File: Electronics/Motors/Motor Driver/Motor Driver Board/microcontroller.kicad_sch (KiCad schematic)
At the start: 65 parts, among them IC301 TJA1057GT/3, IC302 STM32H723ZGT6, J301 TC2030, J302 Screw_Terminal_01x03, J303 TYPE-C-31-M-12, SW301 SW_DIP_x02, U301 USBLC6-4SC6-ES, U302 LSM6DS3, U303 USBLC6-4SC6-ES, X301 25MHz_Clock, X302 32.768kHz_Clock

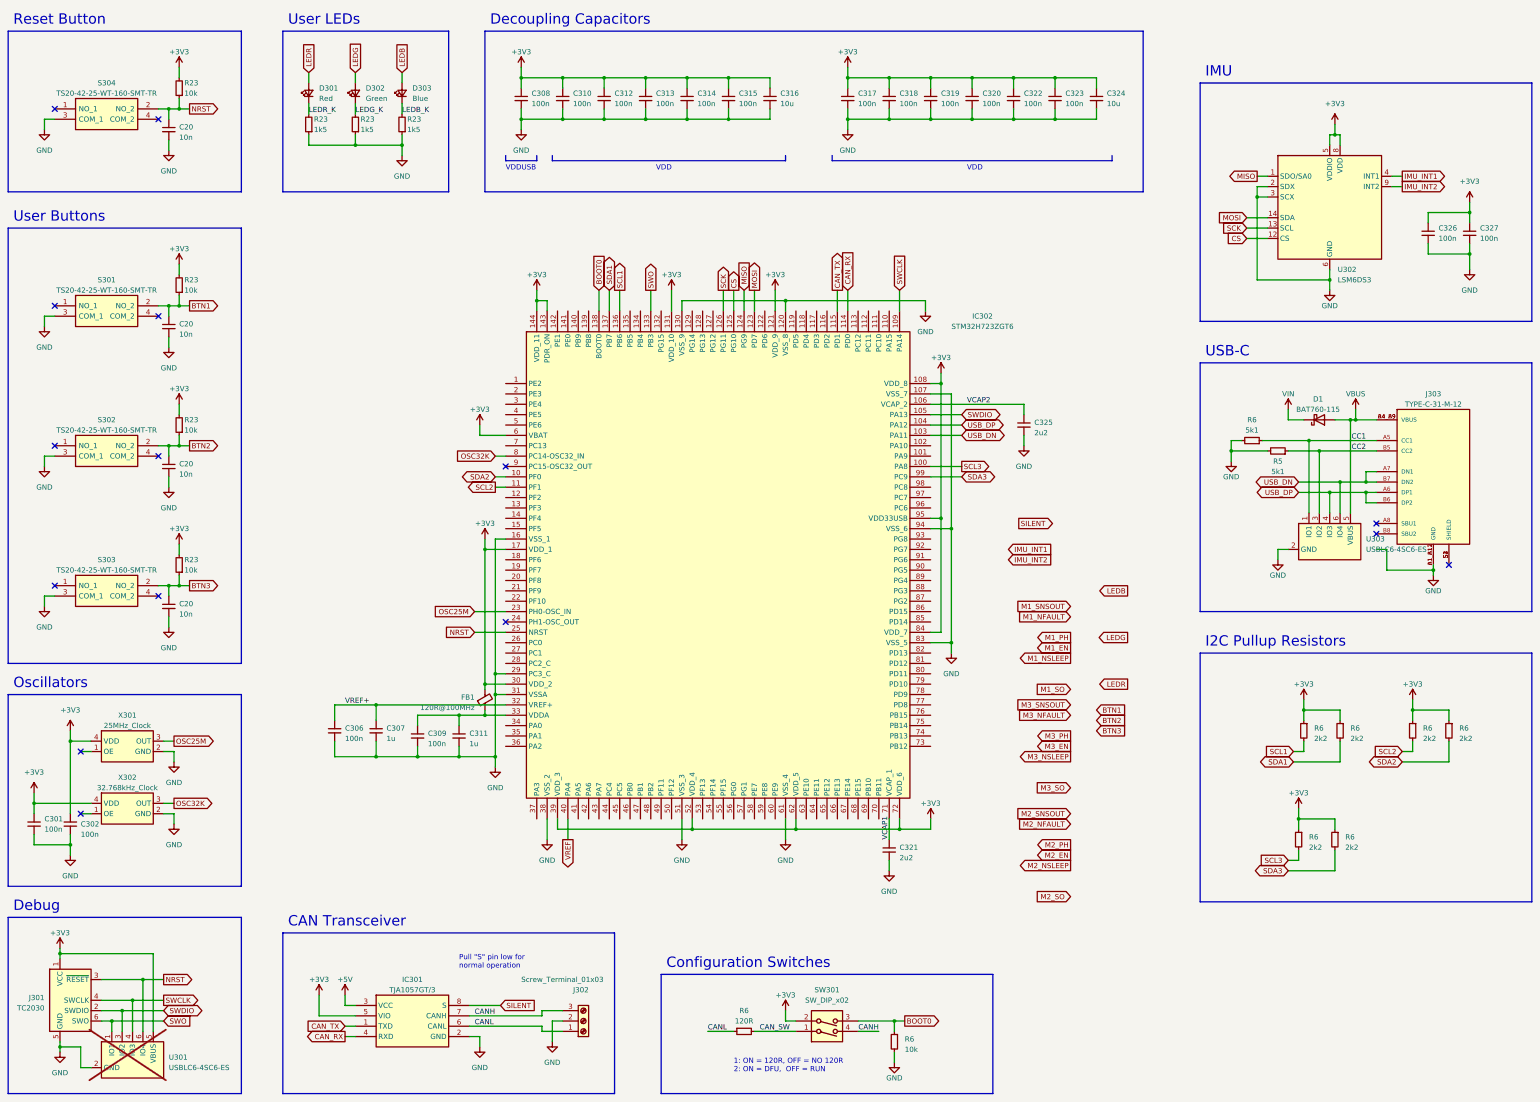
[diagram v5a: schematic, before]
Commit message: Gateway board layout complete and routing begun
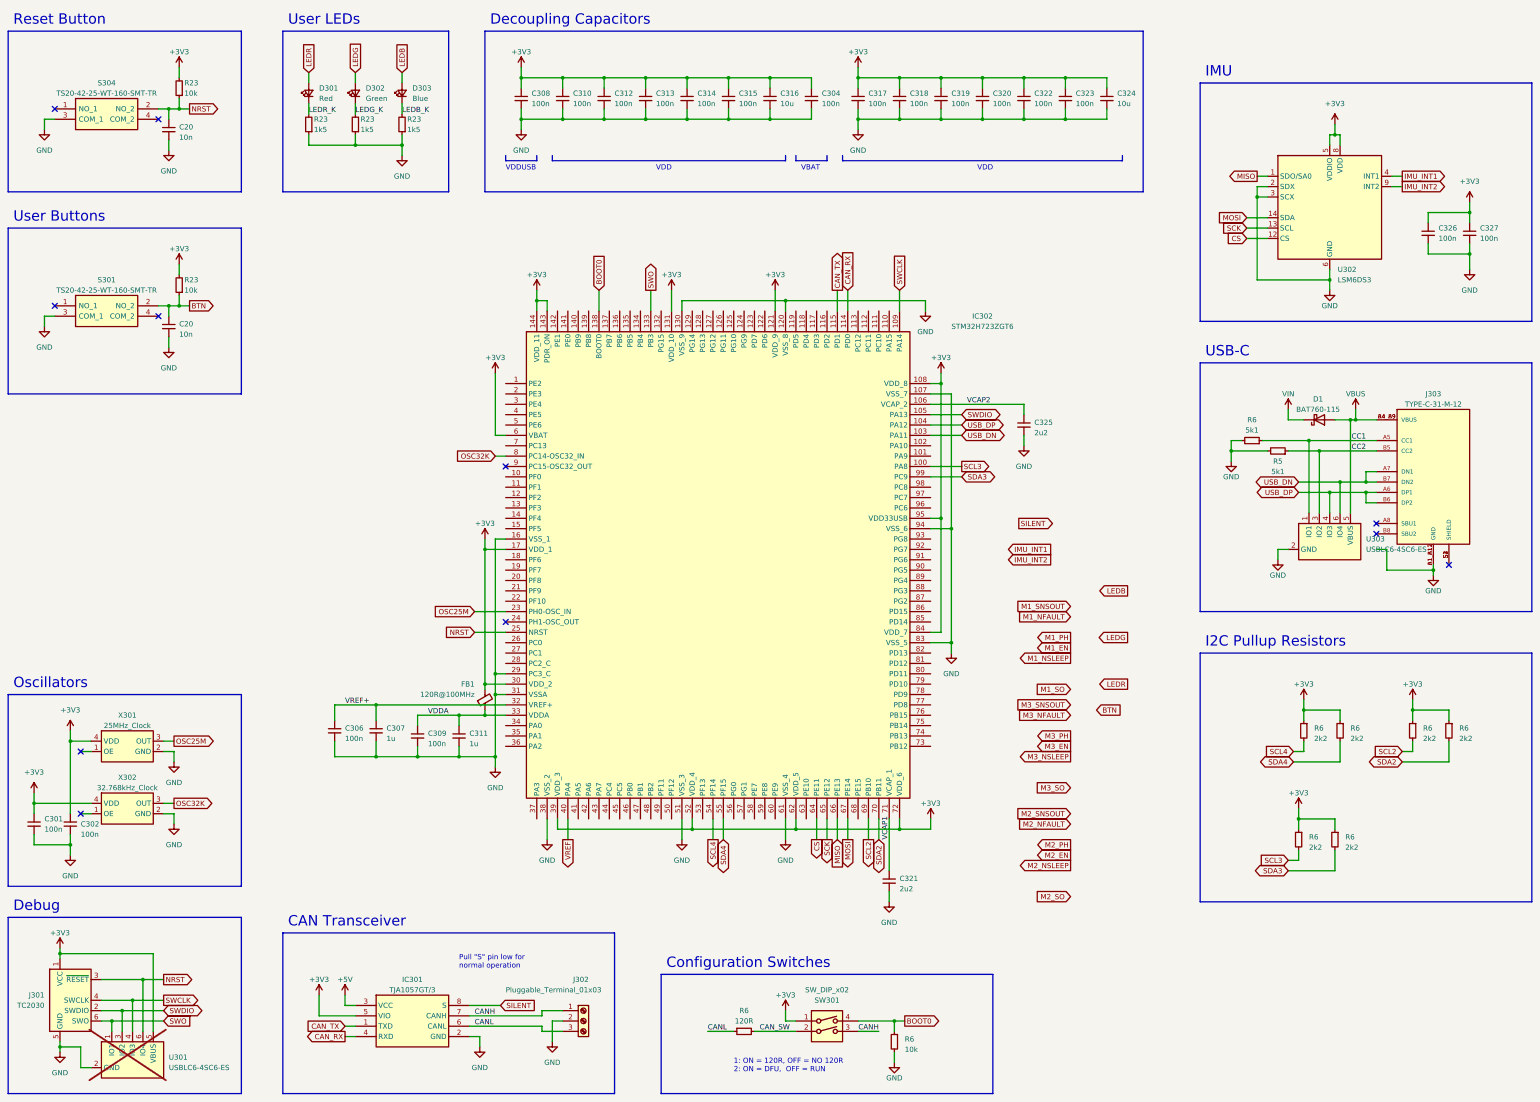
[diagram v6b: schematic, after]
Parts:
- removed C20 (x2): 10n, Capacitor_SMD:C_0402_1005Metric, symbol Device:C_Small
- removed J301: TC2030, Connector:Tag-Connect_TC2030-IDC-FP_2x03_P1.27mm_Vertical, symbol Connector:Conn_ARM_SWD_TagConnect_TC2030
- removed J302: Screw_Terminal_01x03, TerminalBlock:TerminalBlock_bornier-3_P5.08mm, symbol Connector:Screw_Terminal_01x03
- removed R23 (x2): 10k, Resistor_SMD:R_0402_1005Metric, symbol Device:R_Small
- removed S302, S303: TS20-42-25-WT-160-SMT-TR, MSL Footprints:TS204225WT160SMTTRMSL, symbol TS20-42-25-WT-160-SMT-TR-MSL:TS20-42-25-WT-160-SMT-TR
- added C304: 100n, Capacitor_SMD:C_0402_1005Metric, symbol Device:C_Small
- added J301: TC2030, MSL Footprints:Tag-Connect_TC2030-IDC-FP_2x03_P1.27mm_Vertical, symbol MSL_Symbols:TC2030
- added J302: Pluggable_Terminal_01x03, MSL Footprints:Pluggable_terminal-3_P5.08mm, symbol MSL_Symbols:Pluggable_Terminal_01x03
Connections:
- net +3V3: now also SW301.1, C304.1, J301.1 (VCC); no longer SW301.2
- net BOOT0: now also SW301.4; no longer SW301.3
- net CANH: now also SW301.3, J302.1 (Pin_1); no longer SW301.4
- net CANL: now also J302.3 (Pin_3)
- net CAN_SW: now also SW301.2; no longer SW301.1
- net CS: now also IC302.64 (PE11); no longer IC302.125 (PG10)
- net GND: now also C304.2, J301.5 (GND), J302.2 (Pin_2)
- net MISO: now also IC302.66 (PE13); no longer IC302.124 (PG9)
- net MOSI: now also IC302.67 (PE14); no longer IC302.123 (PD7)
- net NRST: now also J301.3 (~{RESET})
- net SCK: now also IC302.65 (PE12); no longer IC302.126 (PG11)
- net SCL2: now also IC302.69 (PB10); no longer IC302.11 (PF1)
- net SDA2: now also IC302.70 (PB11); no longer IC302.10 (PF0)
- net SWCLK: now also J301.4 (SWCLK)
- net SWDIO: now also J301.2 (SWDIO)
- net SWO: now also J301.6 (SWO)
- net VDDA: now reaches C309.1, C311.1, FB1.1, IC302.33 (VDDA)
- net SCL4: now reaches IC302.54 (PF14)
- net SCL4: now also R6.2
- net SDA4: now reaches IC302.55 (PF15)
- net SDA4: now also R6.2
- net BTN1 renamed BTN
- net SCL1: no longer names the net of IC302.136 (PB6)
- net SCL1: no longer R6.2
- net SDA1: no longer names the net of IC302.137 (PB7)
- net SDA1: no longer R6.2
- no-connect marks 15 -> 11
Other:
- note added: "VBAT"
- moved on the sheet: C317, C318, C319, C320, C321, C322, C323, C324

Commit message: Sensor hub board done
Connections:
- net CC1: now also U303.3 (IO2); no longer U303.1 (IO1)
- net CC2: now also U303.1 (IO1); no longer U303.3 (IO2)
- net CS: no longer IC302.64 (PE11)
- net M1_EN: now also IC302.35 (PA1)
- net M1_NFAULT: now also IC302.37 (PA3)
- net M1_NSLEEP: now also IC302.36 (PA2)
- net M1_PH: now also IC302.34 (PA0)
- net M1_SNSOUT: now also IC302.41 (PA5)
- net M1_SO: now also IC302.42 (PA6)
- net M2_EN: now also IC302.64 (PE11)
- net M2_NFAULT: now also IC302.74 (PB13)
- net M2_NSLEEP: now also IC302.65 (PE12)
- net M2_PH: now also IC302.60 (PE9)
- net M2_SNSOUT: now also IC302.73 (PB12)
- net M2_SO: now also IC302.46 (PB0)
- net M3_EN: now also IC302.76 (PB15)
- net M3_NFAULT: now also IC302.79 (PD10)
- net M3_NSLEEP: now also IC302.77 (PD8)
- net M3_PH: now also IC302.75 (PB14)
- net M3_SNSOUT: now also IC302.78 (PD9)
- net M3_SO: now also IC302.49 (PF11)
- net MISO: no longer IC302.66 (PE13)
- net MOSI: no longer IC302.67 (PE14)
- net SCK: no longer IC302.65 (PE12)
- net USB_DN: now also U303.4 (IO3); no longer U303.6 (IO4)
- net USB_DP: now also U303.6 (IO4); no longer U303.4 (IO3)
- no-connect marks 11 -> 12
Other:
- moved on the sheet: C306, C307, C309, C311

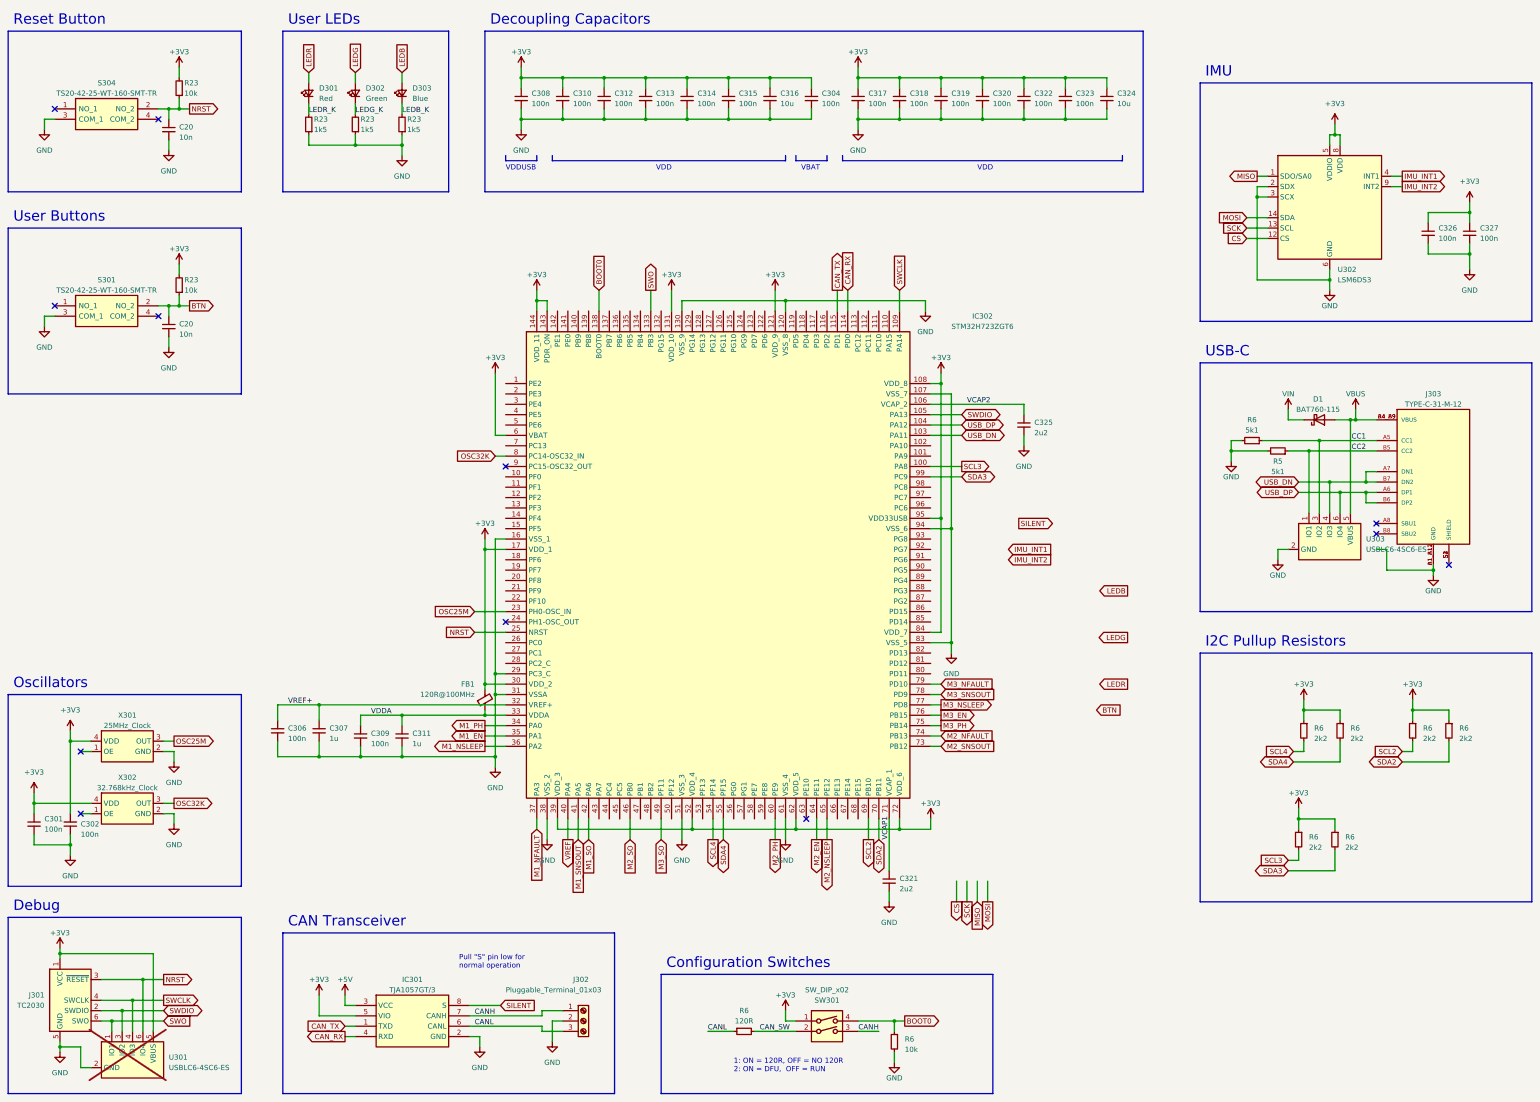
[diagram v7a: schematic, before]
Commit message: Motor driver and power boards done
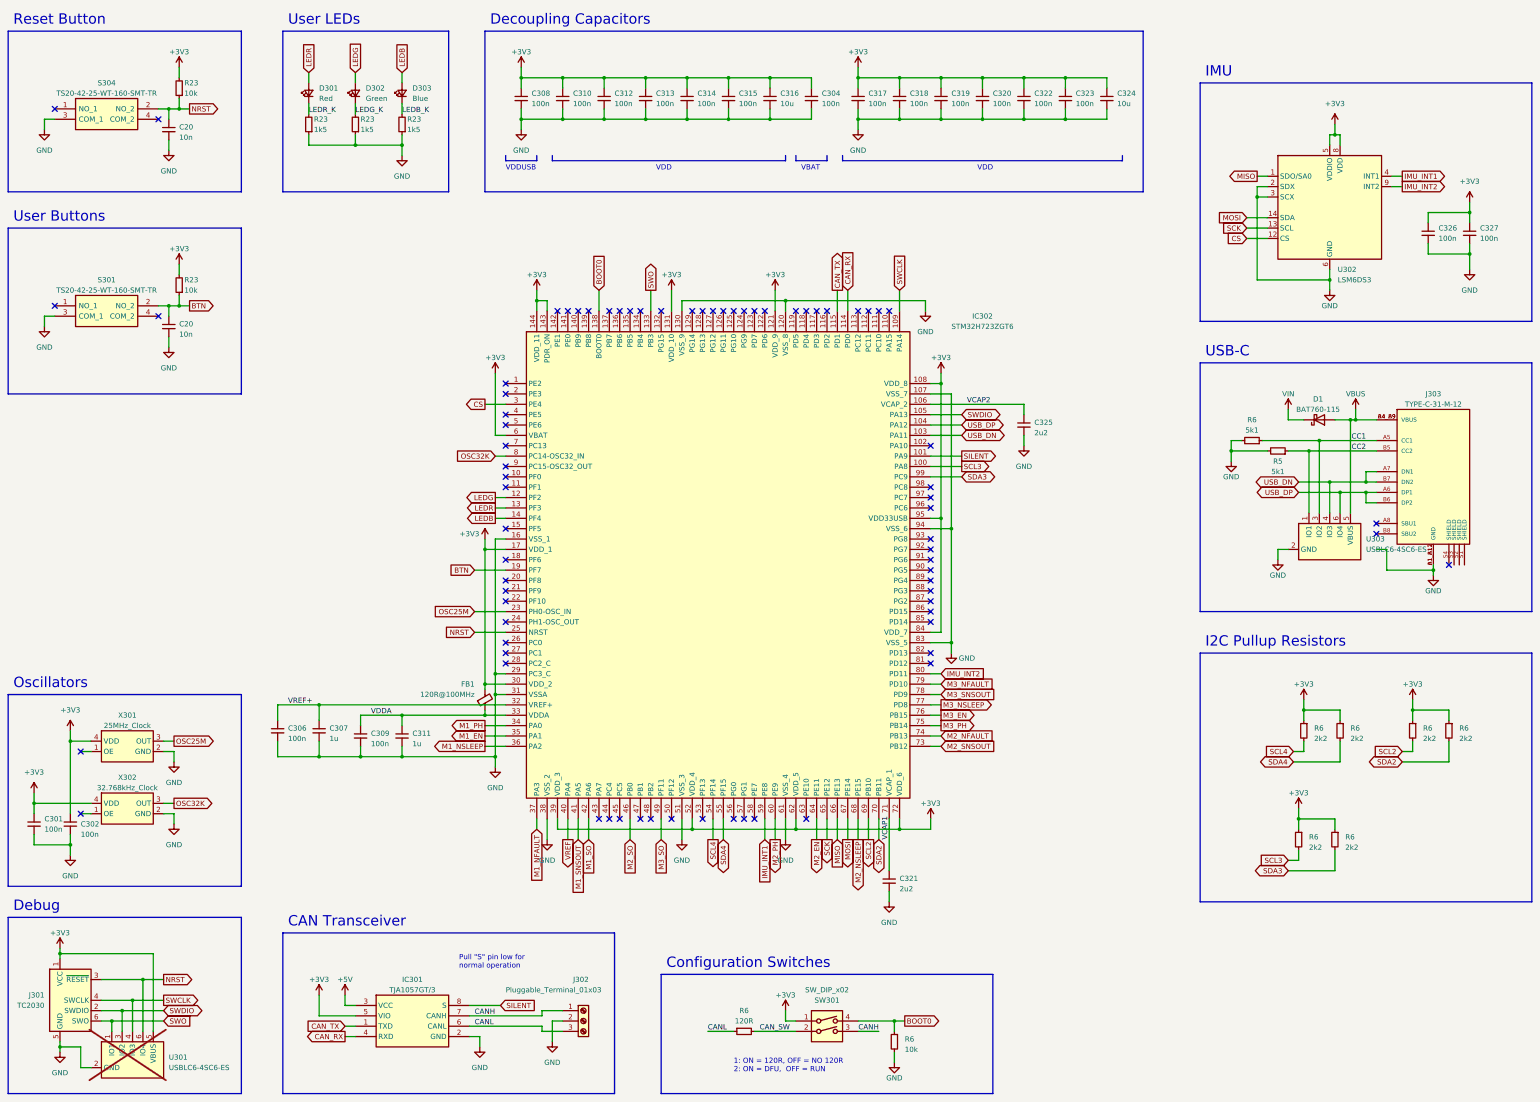
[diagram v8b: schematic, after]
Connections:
- net BTN: now also IC302.19 (PF7)
- net CS: now also IC302.3 (PE4)
- net IMU_INT1: now also IC302.59 (PE8)
- net IMU_INT2: now also IC302.80 (PD11)
- net LEDB: now also IC302.14 (PF4)
- net LEDG: now also IC302.12 (PF2)
- net LEDR: now also IC302.13 (PF3)
- net M2_NSLEEP: now also IC302.68 (PE15); no longer IC302.65 (PE12)
- net MISO: now also IC302.66 (PE13)
- net MOSI: now also IC302.67 (PE14)
- net SCK: now also IC302.65 (PE12)
- net SILENT: now also IC302.101 (PA9)
- now unconnected: J303.S1 (SHIELD), J303.S2 (SHIELD), J303.S3 (SHIELD), J303.S4 (SHIELD)
- no-connect marks 12 -> 77
